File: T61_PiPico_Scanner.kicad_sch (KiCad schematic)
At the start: 18 parts, among them J101 GND, J102 VBUS, J103 EXT5V, J105 GND, J106 PWRSWITCH, U101 Pico

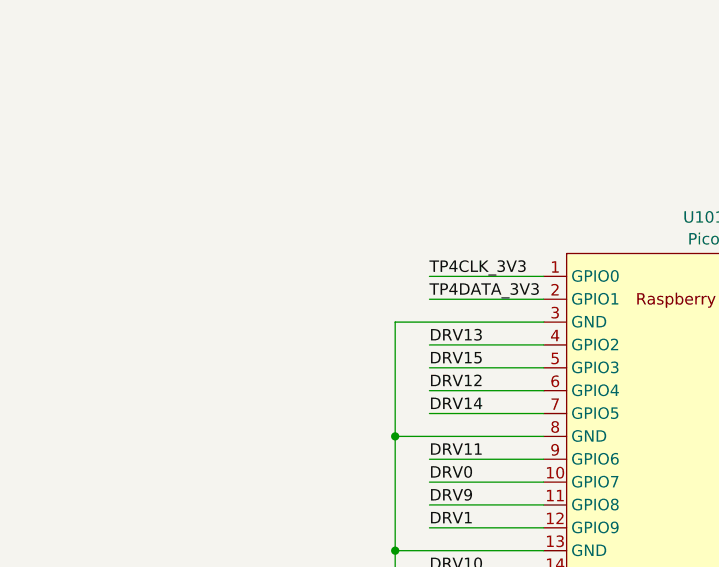
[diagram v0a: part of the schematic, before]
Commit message: rev 1.1: swap PS/2 clk and data for QMK's RP2040 PIO implementation
The only two boards with the wrong order were fixed manually.
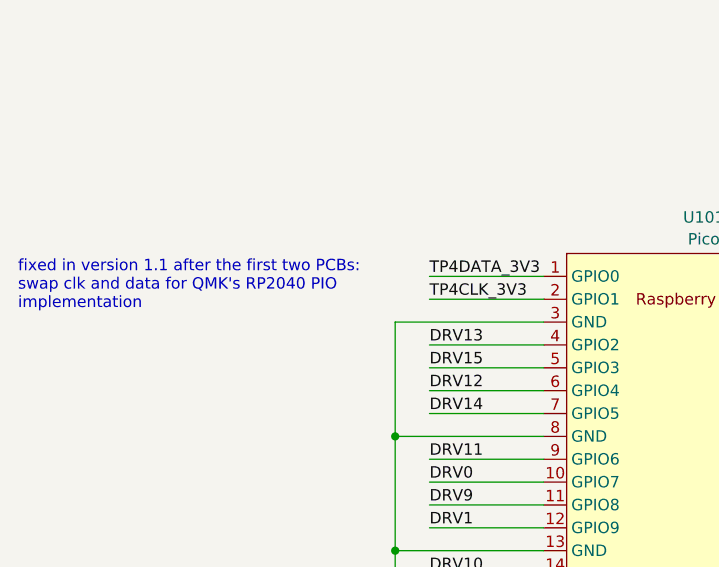
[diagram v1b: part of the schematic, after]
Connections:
- net TP4CLK_3V3: now also U101.2 (GPIO1); no longer U101.1 (GPIO0)
- net TP4DATA_3V3: now also U101.1 (GPIO0); no longer U101.2 (GPIO1)
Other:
- note added: "fixed in version 1.1 after the first two PCBs: swap clk and data for QMK's RP2040 PIO implementation"
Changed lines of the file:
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@@
+    (effects (font (size 1.27 1.27)) (justify left bottom))
+  )
+  (text "fixed in version 1.1 after the first two PCBs:\nswap clk and data for QMK's RP2040 PIO\nimplementation"
+    (at 15.24 72.39 0)
     (effects (font (size 1.27 1.27)) (justify left bottom))
   )
@@
     (effects (font (size 1.27 1.27)) (justify left bottom))
   )
-  (label "TP4CLK_3V3" (at 60.96 68.58 0) (fields_autoplaced)
+  (label "TP4CLK_3V3" (at 60.96 71.12 0) (fields_autoplaced)
     (effects (font (size 1.27 1.27)) (justify left bottom))
   )
@@
     (effects (font (size 1.27 1.27)) (justify left bottom))
   )
-  (label "TP4DATA_3V3" (at 60.96 71.12 0) (fields_autoplaced)
-    (effects (font (size 1.27 1.27)) (justify left bottom))
-  )
+  (label "TP4DATA_3V3" (at 60.96 68.58 0) (fields_autoplaced)
+    (effects (font (size 1.27 1.27)) (justify left bottom))
+  )
